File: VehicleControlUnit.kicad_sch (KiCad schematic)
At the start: 33 parts, among them J1 Conn_01x02, J10 CAR_CAN_OUT, J11 CAR_CAN_Breakout, J2 Precharge_Ready, J4 Precharge+_Conn, J5 Precharge-_Conn, J6 MOTOR_CAN_IN, J7 MOTOR_CAN_OUT, J8 MOTOR_CAN_Breakout, J9 CAR_CAN_IN, Q1 Q_PMOS_GDS

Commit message: first revision
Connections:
- net ISO_ADC_CLK: now also J3.18 (SPI2_MOSI); no longer J3.20 (SPI2_SCK)
- net VPrecharge+: now also J3.20 (SPI2_SCK); no longer J3.18 (SPI2_MOSI)
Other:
- moved on the sheet: H3
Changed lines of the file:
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@@
 	(wire
 		(pts
-			(xy 77.47 99.06) (xy 95.25 99.06)
-		)
-		(stroke
-			(width 0)
-			(type default)
-		)
-	)
-	(wire
-		(pts
 			(xy 232.41 41.91) (xy 232.41 43.18)
 		)
@@
 	(wire
 		(pts
-			(xy 77.47 96.52) (xy 95.25 96.52)
-		)
-		(stroke
-			(width 0)
-			(type default)
-		)
-	)
-	(wire
-		(pts
 			(xy 116.84 93.98) (xy 115.57 93.98)
 		)
@@
 	(wire
 		(pts
+			(xy 77.47 96.52) (xy 95.25 96.52)
+		)
+		(stroke
+			(width 0)
+			(type default)
+		)
+	)
+	(wire
+		(pts
 			(xy 116.84 106.68) (xy 114.3 106.68)
 		)
@@
 	(wire
 		(pts
+			(xy 77.47 99.06) (xy 95.25 99.06)
+		)
+		(stroke
+			(width 0)
+			(type default)
+		)
+	)
+	(wire
+		(pts
 			(xy 151.13 119.38) (xy 149.86 119.38)
 		)
@@
 		)
 	)
-	(label "ISO_ADC_CLK"
-		(at 95.25 96.52 180)
-		(effects
-			(font
-				(size 1.27 1.27)
-			)
-			(justify right bottom)
-		)
-	)
 	(label "M_CAN_H"
 		(at 238.76 31.75 0)
@@
 		)
 	)
+	(label "ISO_ADC_CLK"
+		(at 95.25 99.06 180)
+		(effects
+			(font
+				(size 1.27 1.27)
+			)
+			(justify right bottom)
+		)
+	)
 	(label "M_CAN_L"
 		(at 238.76 34.29 0)
@@
 		)
 	)
+	(label "VPrecharge+"
+		(at 95.25 96.52 180)
+		(effects
+			(font
+				(size 1.27 1.27)
+			)
+			(justify right bottom)
+		)
+	)
 	(label "LED3"
 		(at 162.56 96.52 180)
@@
 		)
 	)
-	(label "VPrecharge+"
-		(at 95.25 99.06 180)
-		(effects
-			(font
-				(size 1.27 1.27)
-			)
-			(justify right bottom)
-		)
-	)
 	(label "LV+"
 		(at 83.82 91.44 180)
@@
 	(symbol
 		(lib_id "Mechanical:MountingHole")
-		(at 188.595 154.94 0)
+		(at 188.595 149.86 0)
 		(unit 1)
 		(exclude_from_sim no)
@@
 		(fields_autoplaced yes)
 		(property "Reference" "H3"
-			(at 191.77 153.6699 0)
+			(at 191.77 148.5899 0)
 			(effects
 				(font
@@
 		)
 		(property "Value" "MountingHole"
-			(at 191.77 156.2099 0)
+			(at 191.77 151.1299 0)
 			(effects
 				(font
@@
 		)
 		(property "Footprint" "MountingHole:MountingHole_3.2mm_M3"
-			(at 188.595 154.94 0)
+			(at 188.595 149.86 0)
 			(effects
 				(font
@@
 		)
 		(property "Datasheet" "~"
-			(at 188.595 154.94 0)
+			(at 188.595 149.86 0)
 			(effects
 				(font
@@
 		)
 		(property "Description" "Mounting Hole without connection"
-			(at 188.595 154.94 0)
+			(at 188.595 149.86 0)
 			(effects
 				(font

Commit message: tweaking
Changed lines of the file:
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@@
 	(text "can make ESP \nenabled all \nthe time to \nsave an LSOM pin"
 		(exclude_from_sim no)
-		(at 107.696 117.348 0)
+		(at 100.33 125.095 0)
 		(effects
 			(font

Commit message: fixed
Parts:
- J10, J2, J4, J5, J9: footprint utsvt_conn:Molex_MicroFit3.0_1x2xP3.00mm_PolarizingPeg_Vertical -> Connector_Molex:Molex_Nano-Fit_105309-xx02_1x02_P2.50mm_Vertical
- J6, J7: footprint utsvt_conn:Molex_MicroFit3.0_1x4xP3.00mm_PolarizingPeg_Vertical -> Connector_Molex:Molex_Nano-Fit_105309-xx04_1x04_P2.50mm_Vertical
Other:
- sheet ContactorDriver ports: added GND; removed LVGND
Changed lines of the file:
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@@
 			)
 		)
-		(property "Footprint" "utsvt_conn:Molex_MicroFit3.0_1x4xP3.00mm_PolarizingPeg_Vertical"
+		(property "Footprint" "Connector_Molex:Molex_Nano-Fit_105309-xx04_1x04_P2.50mm_Vertical"
 			(at 254 29.21 0)
 			(effects
@@
 			)
 		)
-		(property "Footprint" "utsvt_conn:Molex_MicroFit3.0_1x2xP3.00mm_PolarizingPeg_Vertical"
+		(property "Footprint" "Connector_Molex:Molex_Nano-Fit_105309-xx02_1x02_P2.50mm_Vertical"
 			(at 43.18 163.83 0)
 			(effects
@@
 			)
 		)
-		(property "Footprint" "utsvt_conn:Molex_MicroFit3.0_1x2xP3.00mm_PolarizingPeg_Vertical"
+		(property "Footprint" "Connector_Molex:Molex_Nano-Fit_105309-xx02_1x02_P2.50mm_Vertical"
 			(at 129.54 168.91 0)
 			(effects
@@
 			)
 		)
-		(property "Footprint" "utsvt_conn:Molex_MicroFit3.0_1x4xP3.00mm_PolarizingPeg_Vertical"
+		(property "Footprint" "Connector_Molex:Molex_Nano-Fit_105309-xx04_1x04_P2.50mm_Vertical"
 			(at 254 41.91 0)
 			(effects
@@
 			)
 		)
-		(property "Footprint" "utsvt_conn:Molex_MicroFit3.0_1x2xP3.00mm_PolarizingPeg_Vertical"
+		(property "Footprint" "Connector_Molex:Molex_Nano-Fit_105309-xx02_1x02_P2.50mm_Vertical"
 			(at 254 72.39 0)
 			(effects
@@
 			)
 		)
-		(property "Footprint" "utsvt_conn:Molex_MicroFit3.0_1x2xP3.00mm_PolarizingPeg_Vertical"
+		(property "Footprint" "Connector_Molex:Molex_Nano-Fit_105309-xx02_1x02_P2.50mm_Vertical"
 			(at 129.54 154.94 0)
 			(effects
@@
 			)
 		)
-		(property "Footprint" "utsvt_conn:Molex_MicroFit3.0_1x2xP3.00mm_PolarizingPeg_Vertical"
+		(property "Footprint" "Connector_Molex:Molex_Nano-Fit_105309-xx02_1x02_P2.50mm_Vertical"
 			(at 254 64.77 0)
 			(effects
@@
 			)
 		)
-		(pin "LVGND" input
+		(pin "GND" input
 			(at 228.6 123.825 180)
 			(effects

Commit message: review changes
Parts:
- removed J6: MOTOR_CAN_IN, Connector_Molex:Molex_Nano-Fit_105309-xx04_1x04_P2.50mm_Vertical, symbol Connector_Generic:Conn_01x04
- removed J7: MOTOR_CAN_OUT, Connector_Molex:Molex_Nano-Fit_105309-xx04_1x04_P2.50mm_Vertical, symbol Connector_Generic:Conn_01x04
- added J6: Conn_02x04_Counter_Clockwise, utsvt_conn:Molex_MicroFit3.0_2x4xP3.00mm_PolarizingPeg_Vertical, symbol Connector_Generic:Conn_02x04_Counter_Clockwise
- renumbered J11 to J10, J8 to J7, J9 to J8, J10 to J9
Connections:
- net +12V: now also 12V_TP1.1, C2.1, D1.1 (K), J3.21 (12VExt), J3.22 (12VExt), J3.23 (12VExt), J3.24 (12VExt), Q1.2 (D), R4.1, J6.1 (Pin_1), J6.5 (Pin_5); no longer J1.2 (Pin_2), Q1.3 (S)
- net GND: now also J6.2 (Pin_2), J6.6 (Pin_6)
- net LV+: now also J1.2 (Pin_2), Q1.3 (S); no longer 12V_TP1.1, C2.1, D1.1 (K), J3.21 (12VExt), J3.22 (12VExt), J3.23 (12VExt), J3.24 (12VExt), Q1.2 (D), R4.1
- net M_CAN_H: now also J6.3 (Pin_3), J6.7 (Pin_7)
- net M_CAN_L: now also J6.4 (Pin_4), J6.8 (Pin_8)
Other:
- sheet ContactorDriver ports: added none; removed LV+
- moved on the sheet: J7

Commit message: is it time to give up :3
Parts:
- removed J6: Conn_02x04_Counter_Clockwise, utsvt_conn:Molex_MicroFit3.0_2x4xP3.00mm_PolarizingPeg_Vertical, symbol Connector_Generic:Conn_02x04_Counter_Clockwise
- removed J8: CAR_CAN_IN, Connector_Molex:Molex_Nano-Fit_105309-xx02_1x02_P2.50mm_Vertical, symbol Connector_Generic:Conn_01x02
- removed J9: CAR_CAN_OUT, Connector_Molex:Molex_Nano-Fit_105309-xx02_1x02_P2.50mm_Vertical, symbol Connector_Generic:Conn_01x02
- added C3: 0.1u, Capacitor_SMD:C_0805_2012Metric, symbol Device:C
- added J6, J7: Conn_01x04, Connector_Molex:Molex_Nano-Fit_105309-xx04_1x04_P2.50mm_Vertical, symbol Connector_Generic:Conn_01x04
- J4: value Precharge+_Conn -> Conn_01x02
- J5: value Precharge-_Conn -> Conn_01x02
- renumbered J7 to J8, J10 to J9, LV2 to LED1, LV3 to LED2, LV4 to LED3, LV5 to LED4
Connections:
- net +12V: now also C3.1
- net C_CAN_H: now also J6.2 (Pin_2), J6.4 (Pin_4)
- net C_CAN_L: now also J6.1 (Pin_1), J6.3 (Pin_3)
- net GND: now also C3.2
- net ISO_ADC_CLK: now also J4.1 (Pin_1), J5.1 (Pin_1); no longer J4.2 (Pin_2), J5.2 (Pin_2)
- net LED1: now also J3.44 (ADC1_IN3); no longer J3.43 (ADC1_IN12)
- net LED2: now also J3.42 (ADC1_IN2); no longer J3.41 (ADC1_IN11)
- net LED3: now also J3.43 (ADC1_IN12); no longer J3.44 (ADC1_IN3)
- net LED4: now also J3.41 (ADC1_IN11); no longer J3.42 (ADC1_IN2)
- net M_CAN_H: now also J7.2 (Pin_2), J7.4 (Pin_4)
- net M_CAN_L: now also J7.1 (Pin_1), J7.3 (Pin_3)
- net VPrecharge+: now also J4.2 (Pin_2); no longer J4.1 (Pin_1)
- net VPrecharge-: now also J5.2 (Pin_2); no longer J5.1 (Pin_1)
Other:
- moved on the sheet: C2, J8, J9

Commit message: minor fixes
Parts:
- Q1: value Q_PMOS_GDS -> PMV35EPER
- renumbered LV1 to LVPWR1
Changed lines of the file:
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@@
 			)
 		)
-		(property "Value" "Q_PMOS_GDS"
+		(property "Value" "PMV35EPER"
 			(at 62.23 30.48 90)
 			(effects
@@
 			)
 		)
-		(property "Datasheet" "~"
+		(property "Datasheet" "https://assets.nexperia.com/documents/data-sheet/PMV35EPE.pdf"
 			(at 62.23 36.83 0)
 			(effects
@@
 			)
 		)
-		(property "Datasheet" "~"
+		(property "Datasheet" "https://assets.nexperia.com/documents/data-sheet/BZT52-Q_SER.pdf"
 			(at 78.74 43.18 0)
 			(effects
@@
 		(dnp no)
 		(fields_autoplaced yes)
-		(property "Reference" "LV1"
+		(property "Reference" "LVPWR1"
 			(at 110.49 42.2274 90)
 			(effects
@@
 			(project "VehicleControlUnit"
 				(path "/795c8e51-3ded-4d21-b864-aaff31c5def7"
-					(reference "LV1")
+					(reference "LVPWR1")
 					(unit 1)
 				)

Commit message: 24v changes
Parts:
- added J16: Conn_01x08, Connector_PinHeader_2.54mm:PinHeader_1x08_P2.54mm_Vertical, symbol Connector_Generic:Conn_01x08
- R4: value 2k -> 4k
- renumbered 12V_TP1 to 24V_TP1
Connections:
- net 3V3_LSOM: now also J16.5 (Pin_5)
- net GND: now also J4.1 (Pin_1), J5.1 (Pin_1)
- net ISO_ADC_CLK: no longer J4.1 (Pin_1), J5.1 (Pin_1)
- net MPre_Enable: now also J16.2 (Pin_2)
- net MPre_Sense: now also J16.4 (Pin_4)
- net M_Enable: now also J16.1 (Pin_1)
- net M_Sense: now also J16.3 (Pin_3)
- net Precharge_Ready: now also J16.8 (Pin_8)
- net VPrecharge+: now also J16.6 (Pin_6)
- net VPrecharge-: now also J16.7 (Pin_7)
- net +12V renamed +24V
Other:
- note added: "VPrecharge+/- ISO ADC data signals from precharge board Precharge board expected to use same ADC as amperes board which sends a data signal and takes gnd. Make sure to use the same GND to prevent ground loops"
- note removed: "VPrecharge+/- ISO ADC data signals from precharge board Prob AMC1305M25 ISO ADC (give it a clk signal from LSOM and it will return data one bit at a time 16 bit resolution. approx 1mbps data rate, 78Ksps)"

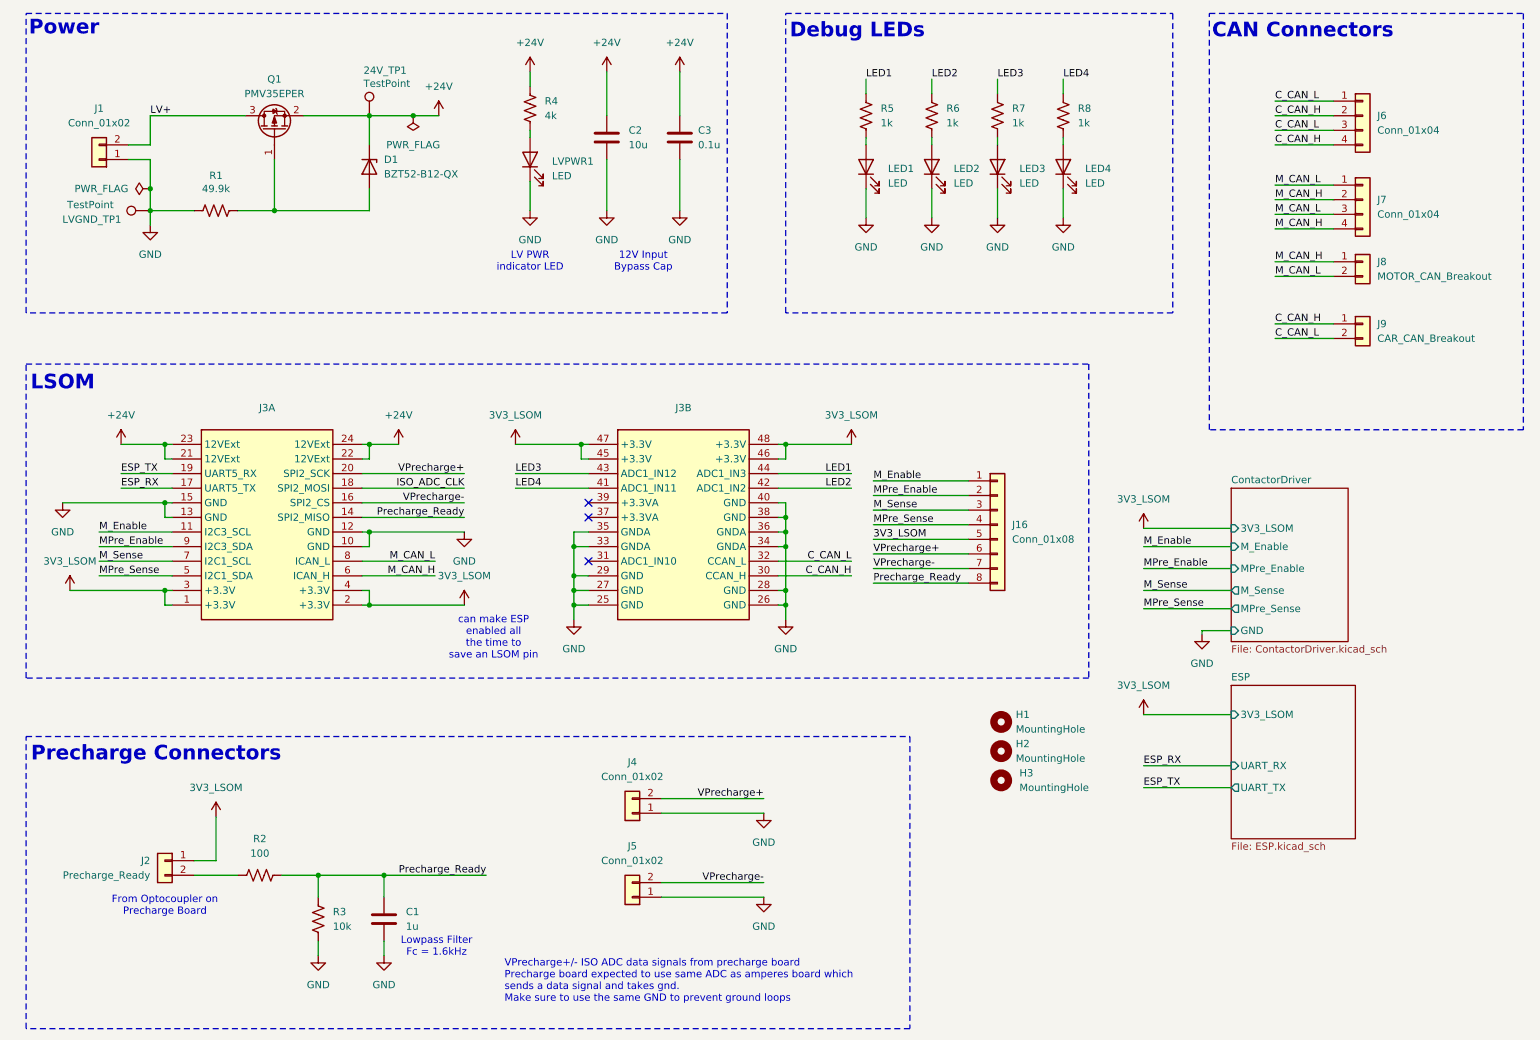
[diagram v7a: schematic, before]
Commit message: moving to kicad-bild
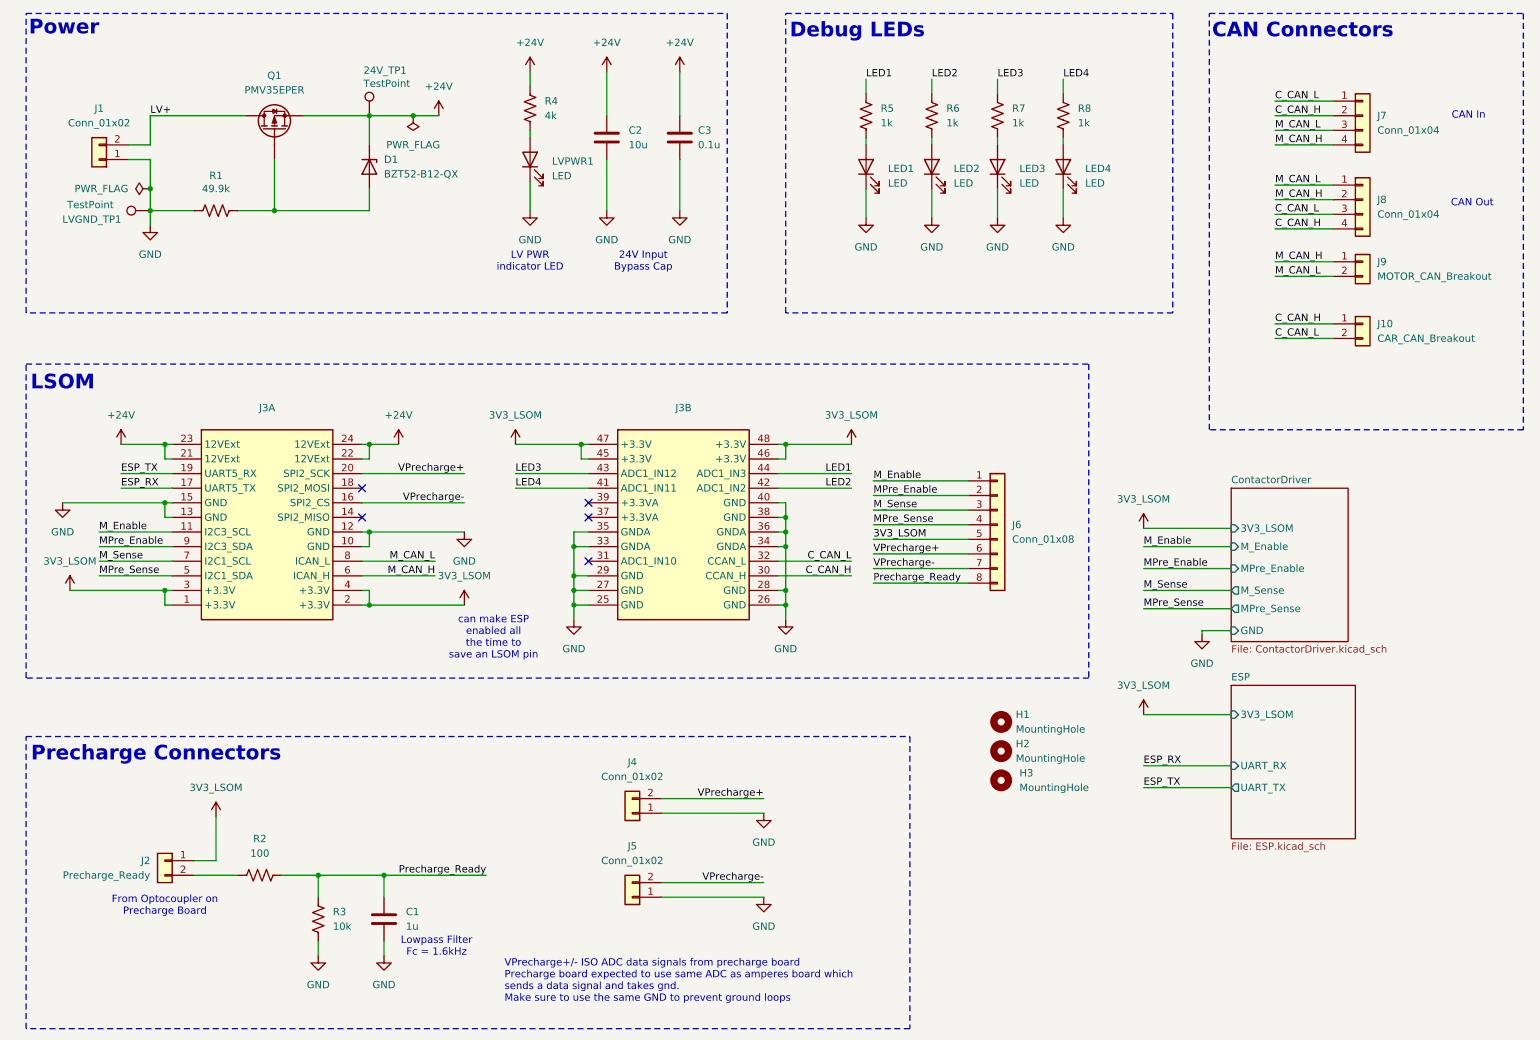
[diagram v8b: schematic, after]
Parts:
- removed J3: ~, UTSVT_Special:LeaderSOM, symbol utsvt-conn:LSOM_DaughterConn
- removed Q1: PMV35EPER, Package_TO_SOT_SMD:SOT-23-3, symbol Device:Q_PMOS_GDS
- added J3: ~, symbol UTSVT_Connectors:LSOM_DaughterConn
- added Q1: PMV35EPER, Package_TO_SOT_SMD:SOT-23-3, symbol Device:Q_PMOS
- renumbered J9 to J10, J16 to J6, J6 to J7, J7 to J8, J8 to J9
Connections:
- net +24V: now also J3.21 (12VExt), J3.22 (12VExt), J3.23 (12VExt), J3.24 (12VExt), Q1.S
- net 3V3_LSOM: now also J3.1 (+3.3V), J3.2 (+3.3V), J3.3 (+3.3V), J3.4 (+3.3V), J3.45 (+3.3V), J3.46 (+3.3V), J3.47 (+3.3V), J3.48 (+3.3V)
- net C_CAN_H: now also J8.4 (Pin_4), J3.30 (CCAN_H); no longer J7.4 (Pin_4)
- net C_CAN_L: now also J8.3 (Pin_3), J3.32 (CCAN_L); no longer J7.3 (Pin_3)
- net ESP_RX: now also J3.17 (UART5_TX)
- net ESP_TX: now also J3.19 (UART5_RX)
- net GND: now also J3.10 (GND), J3.12 (GND), J3.13 (GND), J3.15 (GND), J3.25 (GND), J3.26 (GND), J3.27 (GND), J3.28 (GND), J3.29 (GND), J3.33 (GNDA), J3.34 (GNDA), J3.35 (GNDA), J3.36 (GNDA), J3.38 (GND), J3.40 (GND)
- net LED1: now also J3.44 (ADC1_IN3)
- net LED2: now also J3.42 (ADC1_IN2)
- net LED3: now also J3.43 (ADC1_IN12)
- net LED4: now also J3.41 (ADC1_IN11)
- net LV+: now also Q1.D
- net MPre_Enable: now also J3.9 (I2C3_SDA)
- net MPre_Sense: now also J3.5 (I2C1_SDA)
- net M_CAN_H: now also J7.4 (Pin_4), J3.6 (ICAN_H); no longer J8.4 (Pin_4)
- net M_CAN_L: now also J7.3 (Pin_3), J3.8 (ICAN_L); no longer J8.3 (Pin_3)
- net M_Enable: now also J3.11 (I2C3_SCL)
- net M_Sense: now also J3.7 (I2C1_SCL)
- net VPrecharge+: now also J3.20 (SPI2_SCK)
- net VPrecharge-: now also J3.16 (SPI2_CS)
- net at D1.2 (A), R1.2: now also Q1.G
- no-connect marks 3 -> 5
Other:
- note added: "24V Input Bypass Cap"
- note added: "CAN In"
- note added: "CAN Out"
- note removed: "12V Input Bypass Cap"
